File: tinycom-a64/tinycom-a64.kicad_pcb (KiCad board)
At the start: 4 copper layers, 41.7 x 40.9 mm, 25 parts, among them P1 CONN_02X10, P2 CONN_02X10, U1 AllWinner-A64(FBGA396), U2 H5TQG63BFR/FBGA96

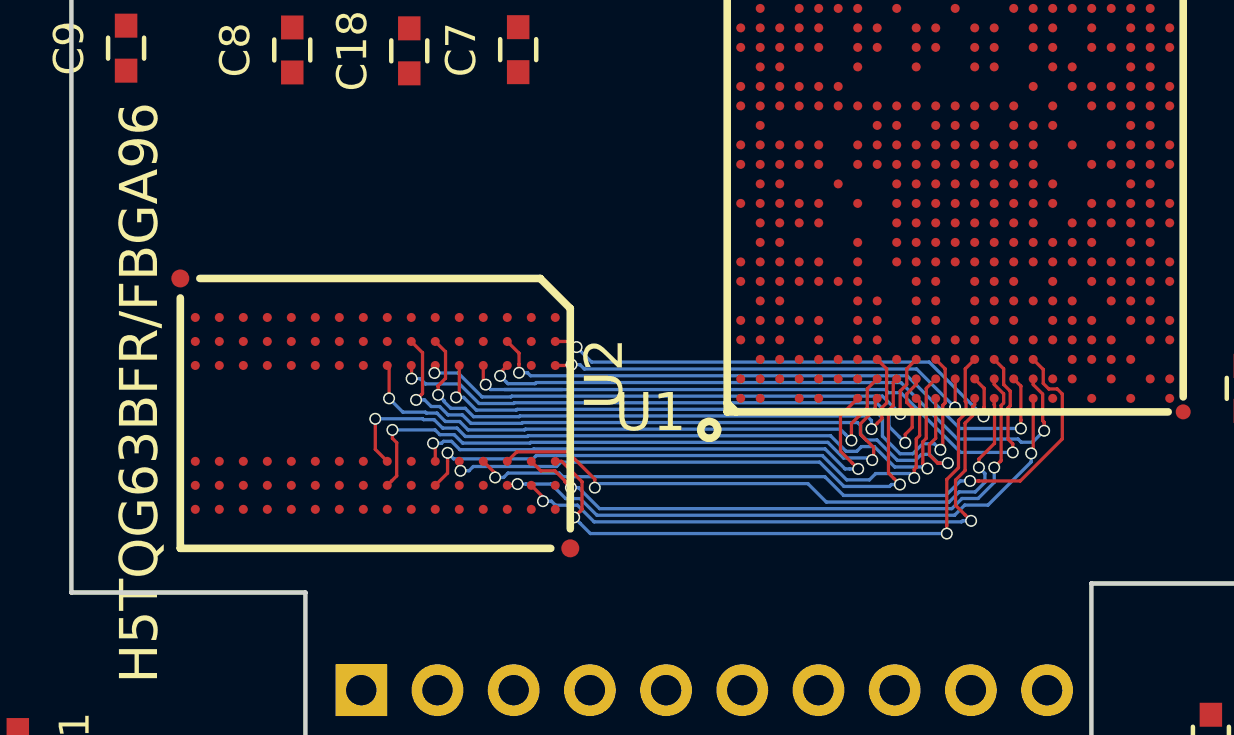
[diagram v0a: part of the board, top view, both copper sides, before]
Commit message: a64 ddr routing
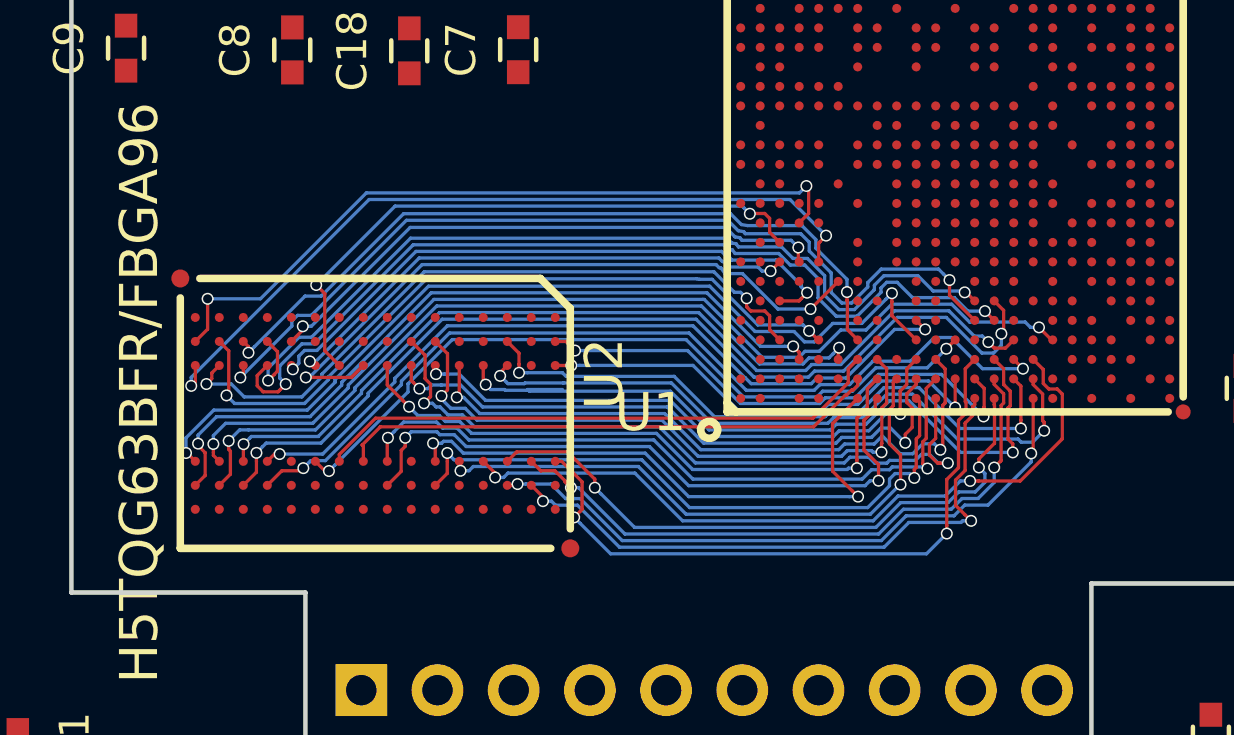
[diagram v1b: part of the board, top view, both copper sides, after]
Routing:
- net SA11: track 0.00 -> 32.9 mm, vias 0 -> 2
- net SA4: track 0.00 -> 31.9 mm, vias 0 -> 2
- net SA0: track 0.00 -> 30.6 mm, vias 0 -> 2
- net SA2: track 0.00 -> 30.5 mm, vias 0 -> 2
- net SA1: track 0.00 -> 30.4 mm, vias 0 -> 2
- net SA14: track 0.00 -> 29.9 mm, vias 0 -> 2
- net SBA1: track 0.00 -> 29.7 mm, vias 0 -> 2
- net SA3: track 0.00 -> 29.6 mm, vias 0 -> 2
- net SA13: track 0.00 -> 26.1 mm, vias 0 -> 2
- net SA12: track 0.00 -> 25.8 mm, vias 0 -> 2
- net SA5: track 0.00 -> 25.5 mm, vias 0 -> 2
- net SA6: track 0.00 -> 25.3 mm, vias 0 -> 2
- net SA10: track 0.00 -> 25.1 mm, vias 0 -> 2
- net SA8: track 0.00 -> 25.0 mm, vias 0 -> 2
- net SRST: track 0.00 -> 24.5 mm, vias 0 -> 2
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
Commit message: route
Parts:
- added C1: C_Small, Capacitors_SMD:C_0603, F.Cu at (115.0, 131.3)
- added C2: C_Small, Capacitors_SMD:C_0603, F.Cu at (109.7, 131.3)
- added Y1: Crystal, Crystals:crystal_FA238-TSX3225, F.Cu at (112.3, 131.2)
- moved R1 21.4 mm to (93.7, 153.9)
- moved C20 1.72 mm to (107.2, 129.6)
- moved C19 1.39 mm to (105.8, 129.6)
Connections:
- P1 pad 14: (no net) -> UD2_N
- P1 pad 16: (no net) -> UD2_P
- P1 pad 6: (no net) -> UD0_N
- P1 pad 8: (no net) -> UD0_P
- P2 pad 10: (no net) -> SDC0_D1
- P2 pad 12: (no net) -> SDC0_D0
- P2 pad 14: (no net) -> SDC0_CLK
- P2 pad 16: (no net) -> SDC0_CMD
- P2 pad 18: (no net) -> SDC0_D3
- P2 pad 20: (no net) -> SDC0_D2
- U1 pad A22: (no net) -> UD0_P
- U1 pad AB10: (no net) -> SDC0_D1
- U1 pad AB6: (no net) -> SDC0_D3
- U1 pad AB9: (no net) -> SDC0_D2
- U1 pad AC8: (no net) -> SDC0_CLK
- U1 pad B22: (no net) -> UD0_N
- U1 pad B23: (no net) -> UD2_P
- U1 pad C22: (no net) -> UD2_N
- U1 pad K22: (no net) -> Net-(C2-Pad1)
- U1 pad K23: (no net) -> Net-(C1-Pad1)
- U1 pad W13: (no net) -> SDC0_D0
- U1 pad W9: (no net) -> SDC0_CMD
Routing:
- net UD0_N: track 0.00 -> 48.3 mm, vias 0 -> 1
- net UD0_P: track 0.00 -> 46.9 mm, vias 0 -> 1
- net UD2_P: track 0.00 -> 37.3 mm, vias 0 -> 1
- net UD2_N: track 0.00 -> 36.6 mm, vias 0 -> 1
- net SDC0_D1: track 0.00 -> 26.2 mm, vias 0 -> 1
- net SDC0_CLK: track 0.00 -> 24.1 mm, vias 0 -> 1
- net SDC0_D3: track 0.00 -> 23.5 mm, vias 0 -> 1
- net SCKE0: track 0.00 -> 23.3 mm
- net SDC0_CMD: track 0.00 -> 21.3 mm, vias 0 -> 1
- net SCS0: track 0.00 -> 20.9 mm
- net SDC0_D0: track 0.00 -> 20.5 mm, vias 0 -> 1
- net SDC0_D2: track 0.00 -> 19.3 mm, vias 0 -> 1
- net Net-(C1-Pad1): track 0.00 -> 5.22 mm
- net Net-(C2-Pad1): track 0.00 -> 4.19 mm
- net Net-(R1-Pad1): track 0.00 -> 3.40 mm
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
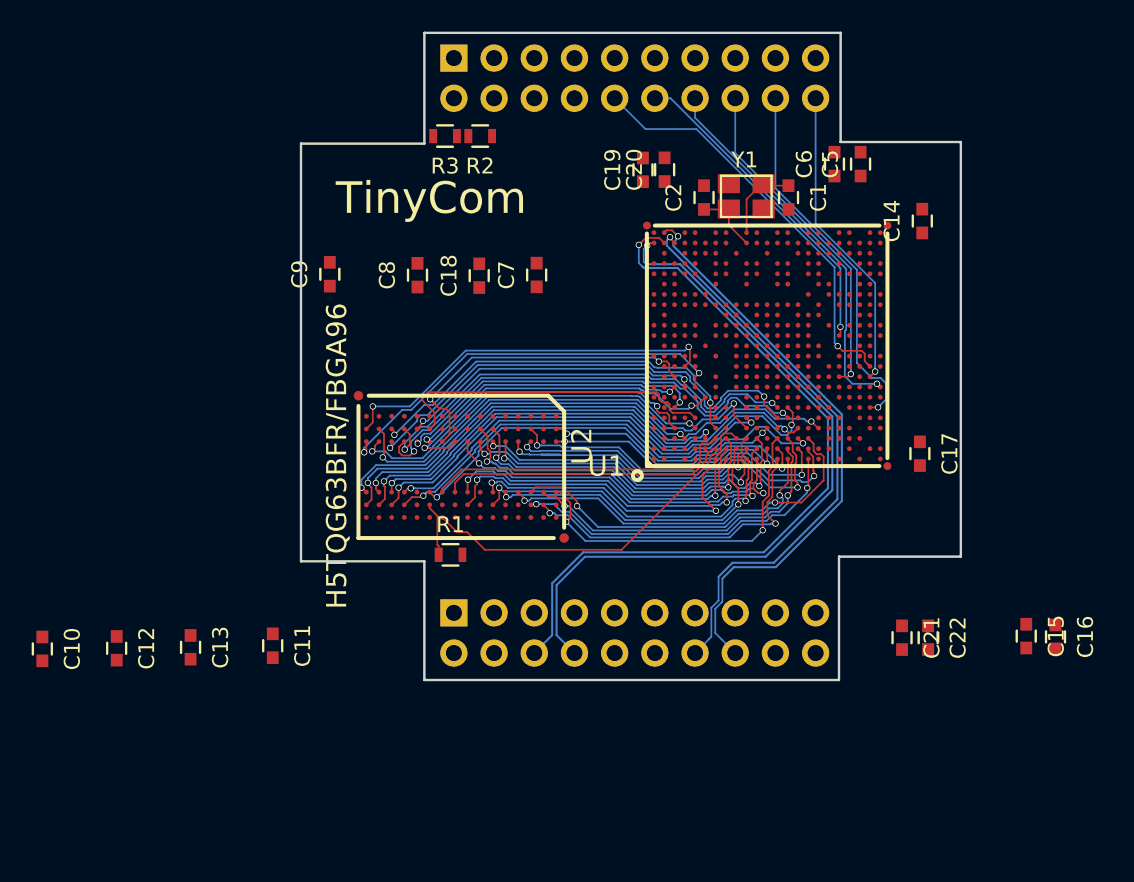
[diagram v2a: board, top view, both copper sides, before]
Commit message: route uart
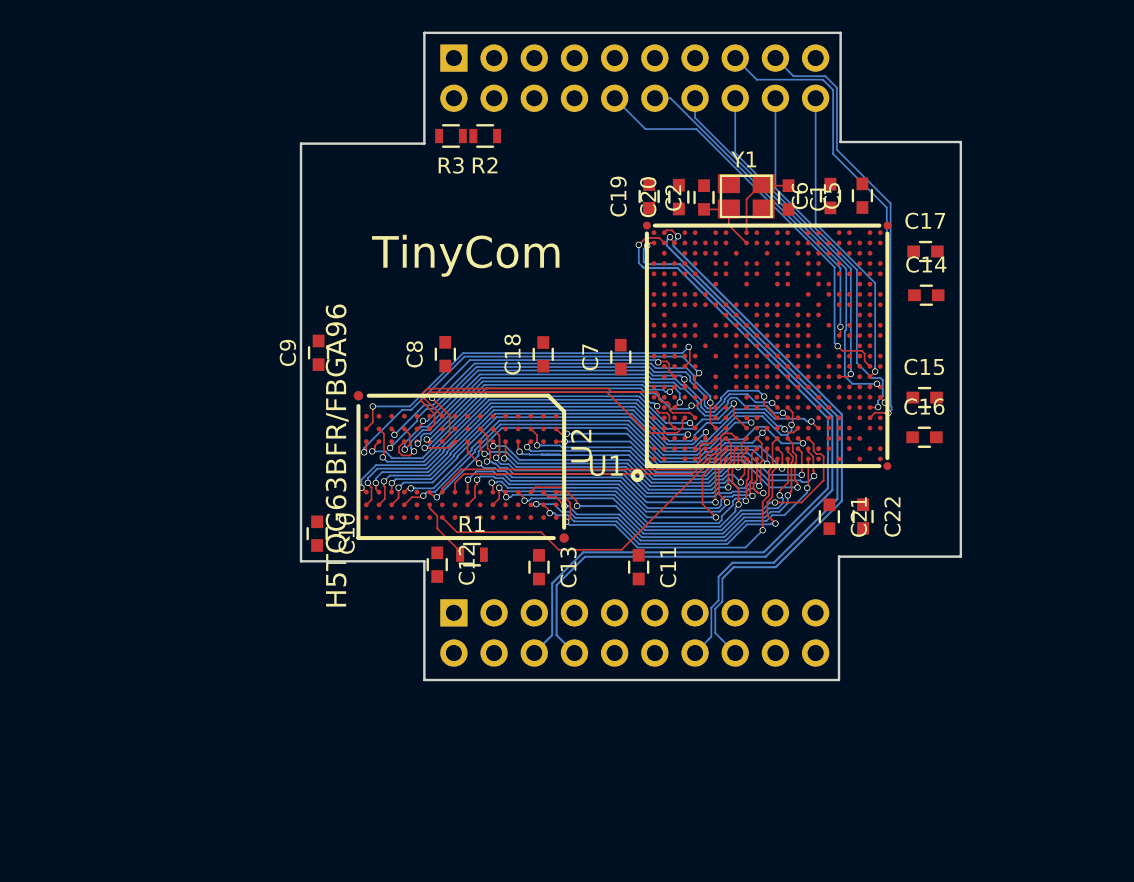
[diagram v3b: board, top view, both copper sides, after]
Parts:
- moved C11 23.7 mm to (105.5, 154.7)
- moved C13 22.6 mm to (99.2, 154.7)
- moved C12 20.9 mm to (92.8, 154.5)
- moved C10 18.8 mm to (85.2, 152.6)
- moved C15 16.4 mm to (123.6, 143.9), turned to 0 degrees
- moved C16 15.1 mm to (123.6, 146.5), turned to 0 degrees
- moved C17 12.8 mm to (123.7, 134.7), turned to 0 degrees
- moved C21 8.92 mm to (117.6, 151.5)
- moved C22 8.69 mm to (119.7, 151.5)
- moved C7 7.43 mm to (104.4, 141.4)
- moved C18 6.41 mm to (99.5, 141.2)
- moved C8 5.30 mm to (93.3, 141.2)
- moved C9 5.02 mm to (85.3, 141.1)
- moved C14 4.69 mm to (123.7, 137.5), turned to 0 degrees
- moved C6 2.03 mm to (117.7, 131.2)
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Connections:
- P2 pad 15: (no net) -> UART0_RX
- P2 pad 17: (no net) -> UART0_TX
- U1 pad AB5: (no net) -> UART0_TX
- U1 pad AC7: (no net) -> UART0_RX
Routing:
- net UART0_RX: track 0.00 -> 28.7 mm, vias 0 -> 1
- net UART0_TX: track 0.00 -> 28.0 mm, vias 0 -> 1
- net SODT0: track 0.00 -> 20.0 mm
- net SDQ1: track 19.6 -> 20.2 mm
- net Net-(R1-Pad1): track 3.40 -> 3.95 mm
- net SDQ3: track 21.0 -> 21.5 mm
- net SDQM0: track 19.9 -> 20.4 mm
- net SDQ7: track 23.2 -> 23.7 mm

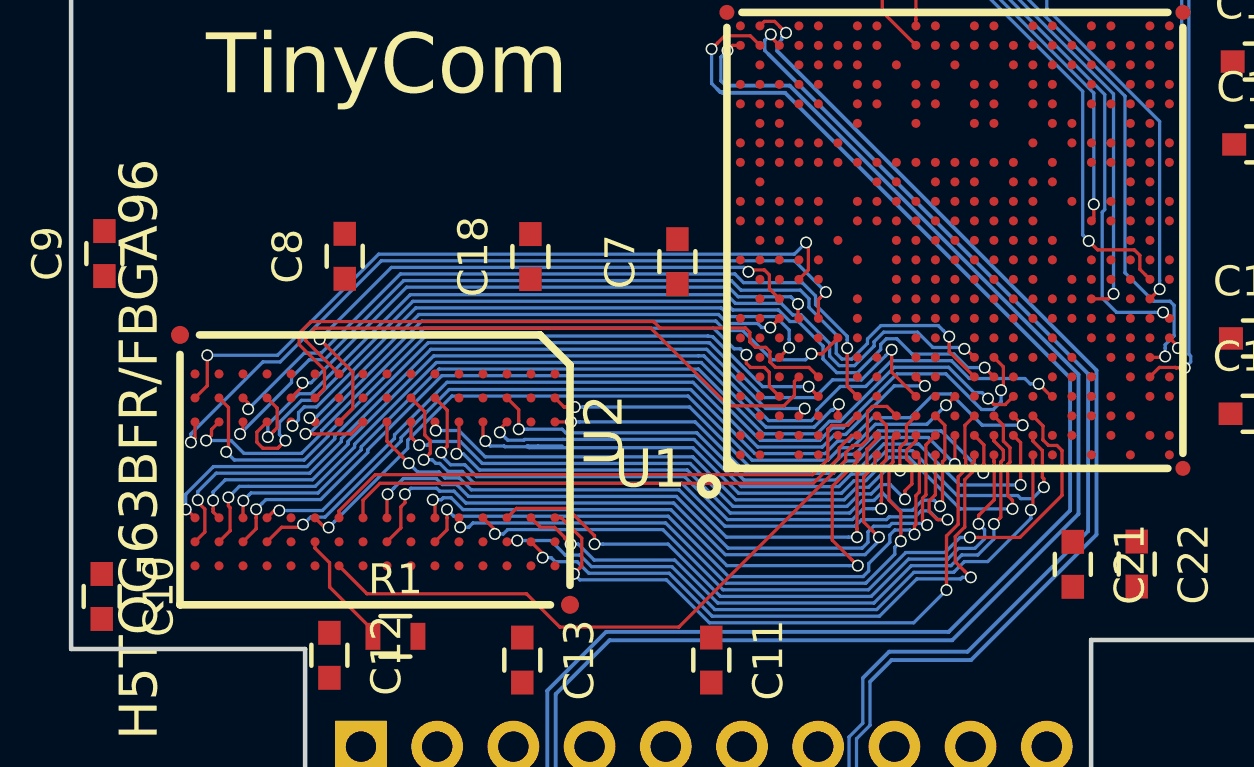
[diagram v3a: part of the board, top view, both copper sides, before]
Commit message: route ddr power
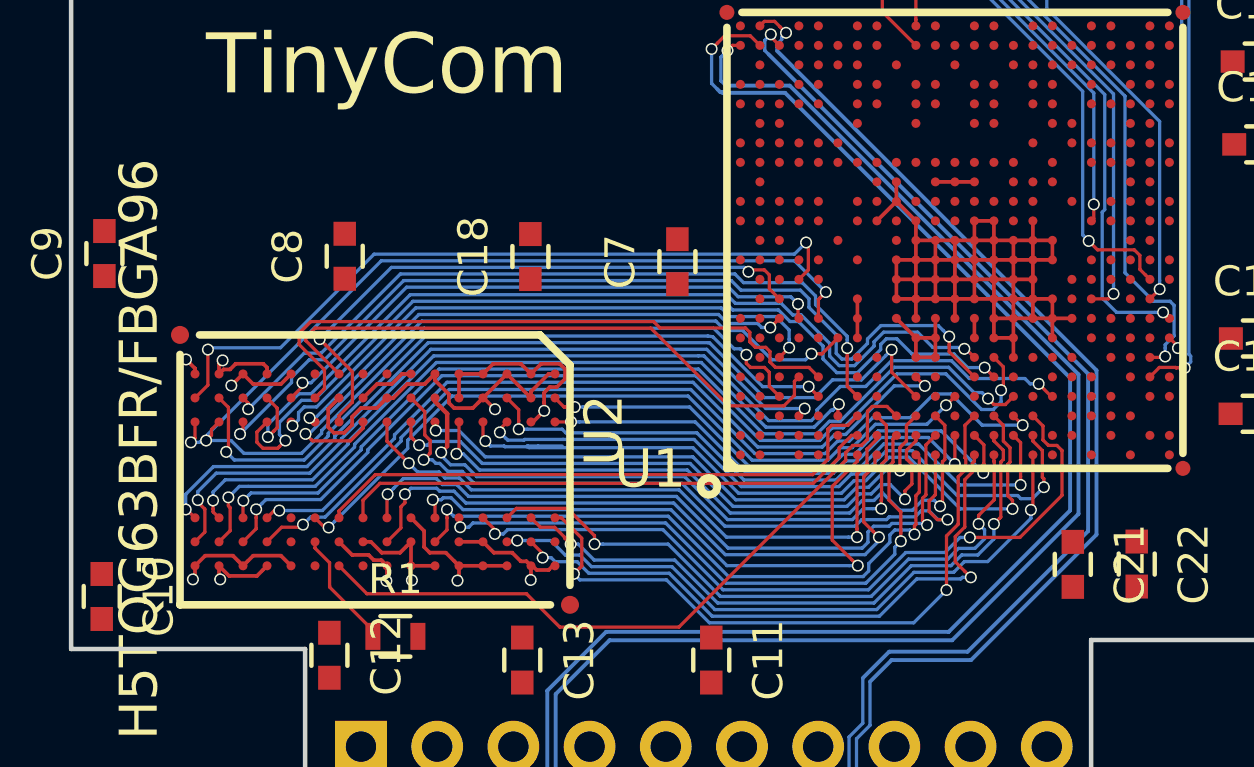
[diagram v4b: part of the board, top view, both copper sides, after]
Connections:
- U1 pad A1: (no net) -> GND
- U1 pad A23: (no net) -> GND
- U1 pad AA1: (no net) -> VCC_12
- U1 pad AA3: (no net) -> VCC_12
- U1 pad AB2: (no net) -> VCC_12
- U1 pad AC1: (no net) -> VCC_12
- U1 pad AC2: (no net) -> VCC_12
- U1 pad AC23: (no net) -> GND
- U1 pad C3: (no net) -> GND
- U1 pad C7: (no net) -> GND
- U1 pad D7: (no net) -> GND
- U1 pad G11: (no net) -> GND
- U1 pad G6: (no net) -> GND
- U1 pad G7: (no net) -> VCC_15
- U1 pad G8: (no net) -> VCC_15
- U1 pad G9: (no net) -> VCC_15
- U1 pad H13: (no net) -> GND
- U1 pad H4: (no net) -> GND
- U1 pad J10: (no net) -> GND
- U1 pad J11: (no net) -> GND
- U1 pad J14: (no net) -> GND
- U1 pad J15: (no net) -> GND
- U1 pad J8: (no net) -> VCC_15
- U1 pad J9: (no net) -> GND
- U1 pad K10: (no net) -> GND
- U1 pad K11: (no net) -> GND
- U1 pad K12: (no net) -> GND
- U1 pad K13: (no net) -> GND
- U1 pad K6: (no net) -> VCC_15
- U1 pad K7: (no net) -> VCC_15
- U1 pad K8: (no net) -> GND
- U1 pad K9: (no net) -> GND
- U1 pad L10: (no net) -> GND
- U1 pad L11: (no net) -> GND
- U1 pad L12: (no net) -> GND
- U1 pad L15: (no net) -> GND
- U1 pad L4: (no net) -> GND
- U1 pad L5: (no net) -> GND
- U1 pad L6: (no net) -> VCC_15
- U1 pad L7: (no net) -> VCC_15
- U1 pad L8: (no net) -> VCC_15
- U1 pad L9: (no net) -> GND
- U1 pad M10: (no net) -> GND
- U1 pad M11: (no net) -> GND
- U1 pad M12: (no net) -> GND
- U1 pad M15: (no net) -> GND
- U1 pad M3: (no net) -> GND
- U1 pad M8: (no net) -> GND
- U1 pad M9: (no net) -> GND
- U1 pad N10: (no net) -> GND
- U1 pad N11: (no net) -> GND
- U1 pad N12: (no net) -> GND
- U1 pad N13: (no net) -> GND
- U1 pad N15: (no net) -> GND
- U1 pad N4: (no net) -> GND
- U1 pad N7: (no net) -> VCC_15
- U1 pad N8: (no net) -> VCC_15
- U1 pad N9: (no net) -> GND
- U1 pad P10: (no net) -> GND
- U1 pad P11: (no net) -> GND
- U1 pad P12: (no net) -> GND
- U1 pad P13: (no net) -> GND
- U1 pad P7: (no net) -> GND
- U1 pad P8: (no net) -> GND
- U1 pad P9: (no net) -> GND
- U1 pad R10: (no net) -> GND
- U1 pad R11: (no net) -> GND
- U1 pad R12: (no net) -> GND
- U1 pad R15: (no net) -> GND
- U1 pad R5: (no net) -> GND
- U1 pad R6: (no net) -> GND
- U1 pad R7: (no net) -> GND
- U1 pad R8: (no net) -> GND
- U1 pad R9: (no net) -> GND
- U1 pad T10: (no net) -> GND
- U1 pad T11: (no net) -> GND
- U1 pad T12: (no net) -> GND
- U1 pad T13: (no net) -> GND
- U1 pad T8: (no net) -> GND
- U1 pad T9: (no net) -> GND
- U1 pad U11: (no net) -> GND
- U1 pad U12: (no net) -> GND
- U1 pad U2: (no net) -> GND
- U1 pad U5: (no net) -> GND
- U1 pad U6: (no net) -> VCC_12
- U1 pad U7: (no net) -> GND
- U1 pad U8: (no net) -> GND
- U1 pad U9: (no net) -> GND
- U1 pad V14: (no net) -> GND
- U1 pad V2: (no net) -> VCC_12
- U1 pad V3: (no net) -> VCC_12
- U1 pad V4: (no net) -> VCC_12
- U1 pad V5: (no net) -> VCC_12
- U1 pad V6: (no net) -> VCC_12
- U1 pad V8: (no net) -> GND
- U1 pad W1: (no net) -> VCC_12
- U1 pad W3: (no net) -> VCC_12
- U1 pad W4: (no net) -> VCC_12
- U1 pad W5: (no net) -> VCC_12
- U1 pad Y2: (no net) -> VCC_12
- U1 pad Y3: (no net) -> VCC_12
- U1 pad Y4: (no net) -> VCC_12
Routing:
- net GND: track 0.00 -> 76.5 mm, vias 0 -> 6
- net VCC_15: track 0.00 -> 30.4 mm, vias 0 -> 5
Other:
- net class Default: clearance 0.11 -> 0.15; trace_width 0.11 -> 0.15
- rule trace_clearance: 0.11 -> 0.15

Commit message: route
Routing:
- net VCC_15: track 30.4 -> 43.2 mm, vias 5 -> 13
- net GND: track 76.5 -> 82.4 mm, vias 6 -> 15
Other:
- net class Default: clearance 0.15 -> 0.125; trace_width 0.15 -> 0.125
- rule trace_clearance: 0.15 -> 0.125

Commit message: route
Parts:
- moved C21 2.62 mm to (120.1, 150.7)
- moved C22 1.75 mm to (118.2, 150.7)
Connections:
- U1 pad J12: (no net) -> VCC_12
- U1 pad J13: (no net) -> VCC_12
- U1 pad K14: (no net) -> VCC_12
- U1 pad L13: (no net) -> VCC_12
- U1 pad L14: (no net) -> VCC_12
- U1 pad L16: (no net) -> VCC_33
- U1 pad M13: (no net) -> VCC_12
- U1 pad M14: (no net) -> VCC_12
- U1 pad N14: (no net) -> VCC_12
- U1 pad P14: (no net) -> VCC_12
- U1 pad R13: (no net) -> VCC_12
- U1 pad R14: (no net) -> VCC_12
- U1 pad T15: (no net) -> VCC_12
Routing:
- net SVREF: track 0.00 -> 49.9 mm, vias 0 -> 4
- net VCC_12: track 0.00 -> 28.3 mm, vias 0 -> 9
- net VCC_33: track 0.00 -> 22.2 mm, vias 0 -> 6
- net VCC_15: track 43.2 -> 57.1 mm, vias 13 -> 15
- net GND: track 82.4 -> 94.2 mm, vias 15 -> 25
- net SODT0: track 20.0 -> 21.2 mm
- net SCS0: track 21.3 -> 22.4 mm
- net SCAS: track 20.5 -> 21.2 mm
- net SA7: track 24.4 -> 24.9 mm
- added copper zone on In2.Cu, net VCC_12
- removed copper zone on In2.Cu, net VCC_33
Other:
- net class Default: clearance 0.125 -> 0.11; trace_width 0.125 -> 0.11
- net class Ground: clearance 0.125 -> 0.11; trace_width 0.125 -> 0.11
- net class Power: clearance 0.125 -> 0.13; trace_width 0.125 -> 0.3
- rule trace_clearance: 0.125 -> 0.11
